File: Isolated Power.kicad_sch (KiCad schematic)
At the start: 3 parts, among them U6 ISU0205S05

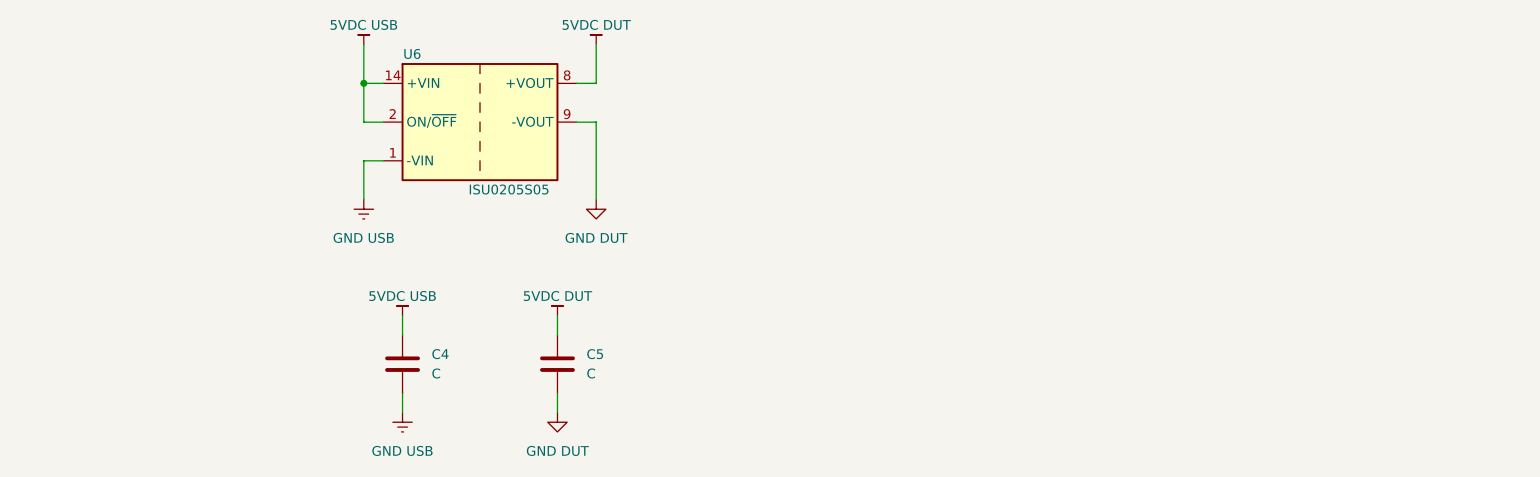
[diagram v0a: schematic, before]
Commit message: Power & Level Translation
Isolated 5VDC changed and a 3.3VDC LDO was added. The original 5VDC was too expensive and big. The new one is still both, but less so.
The level translator is now a dedicated IC instead of MOSFETs. I was having trouble making it work the way I wanted.
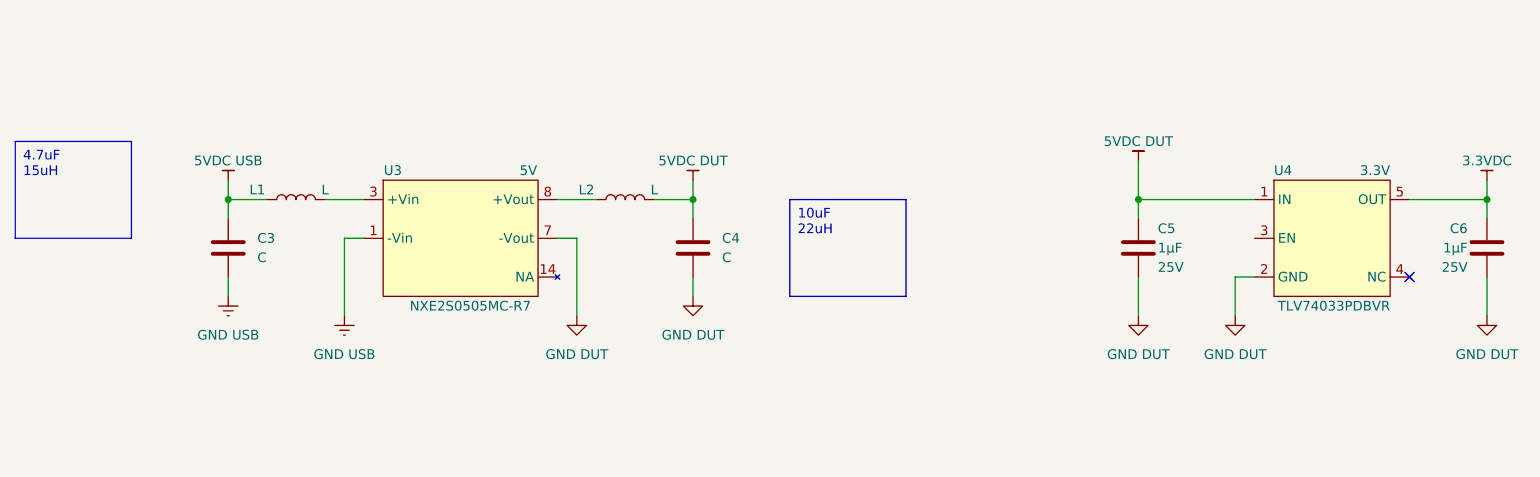
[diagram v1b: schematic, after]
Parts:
- removed U6: ISU0205S05, Converter_DCDC:Converter_DCDC_XP_POWER-ISU02_SMD, symbol Converter_DCDC:ISU0205S05
- added C5, C6: Capacitor Ceramic 1uF 25V X5R 0603, Capacitor_SMD:C_0603_1608Metric, symbol Device:C
- added L1, L2: L, symbol Device:L
- added U3: Regulator SMPS Module Vout=5V±12% Iout=400mA Vin=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, symbol Prototype Schematic Symbols - Isolated ComPort:Regulator SMPS Module 5V±12% 400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
- added U4: Regulator Linear LDO 3.3V±1% 300mA OTP OCP SOT23-5, Package_TO_SOT_SMD:SOT-23-5, symbol Prototype Schematic Symbols - Isolated ComPort:Regulator Linear LDO 3.3V±1% 300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
- renumbered C4 to C3, C5 to C4
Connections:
- net 5VDC DUT: now also C5.1, L2.2, U4.1 (IN)
- net 5VDC USB: now also L1.1
- net GND DUT: now also C5.2, C6.2, U3.7 (-Vout), U4.2 (GND)
- net GND USB: now also U3.1 (-Vin)
- new net: L1.2, U3.3 (+Vin)
- new net: L2.1, U3.8 (+Vout)
- new net 3.3VDC: C6.1, U4.5 (OUT)
- no-connect marks 0 -> 1
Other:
- moved on the sheet: C3, C4
